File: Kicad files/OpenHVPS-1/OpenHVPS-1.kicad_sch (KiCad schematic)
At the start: 64 parts, among them J1 Conn_01x03_Male, Q1 FQT7N10, Q2 BC846, Q3 MMDT3906, U1 74HC14, U2 MAX4162, U3 CD14538BM, U4 MAX6008AEUR+T

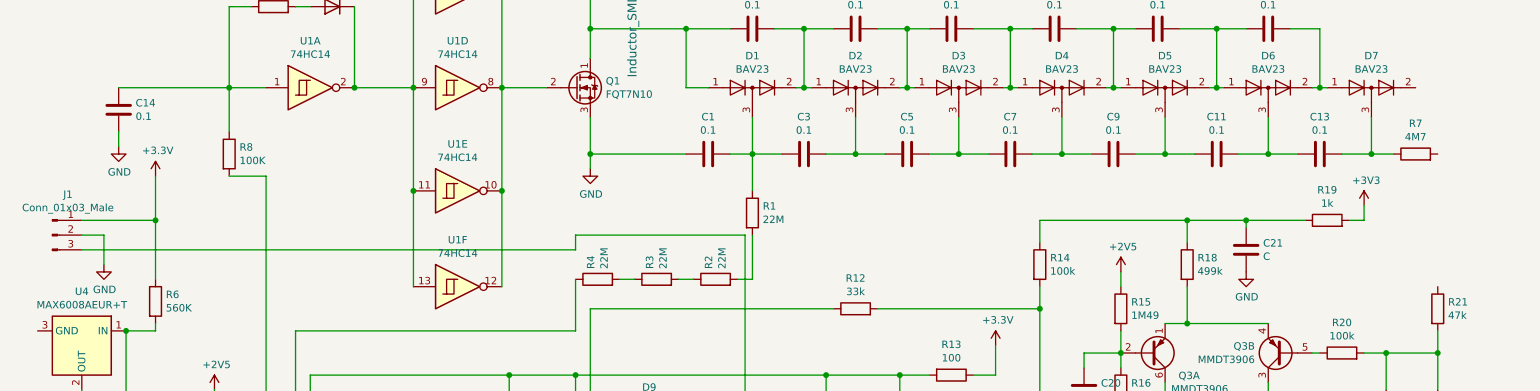
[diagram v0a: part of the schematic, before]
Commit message: Added extra outputs and A-C placement moved
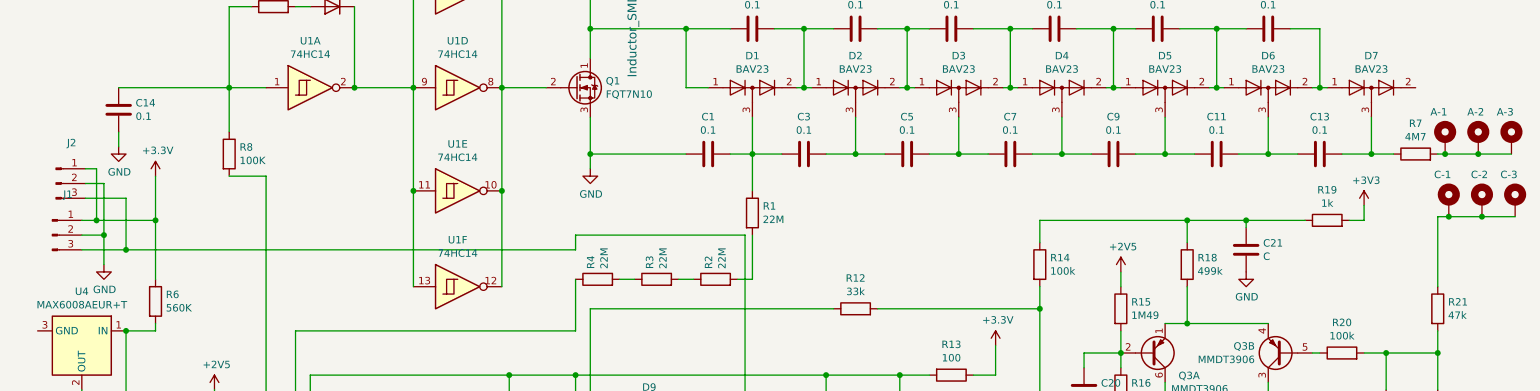
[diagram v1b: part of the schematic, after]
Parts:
- added H1: A-1, TestPoint:TestPoint_Loop_D1.80mm_Drill1.0mm_Beaded, symbol Mechanical:MountingHole_Pad
- added H2: C-1, TestPoint:TestPoint_Loop_D1.80mm_Drill1.0mm_Beaded, symbol Mechanical:MountingHole_Pad
- added H3: A-2, TestPoint:TestPoint_Loop_D2.60mm_Drill1.4mm_Beaded, symbol Mechanical:MountingHole_Pad
- added H4: C-2, TestPoint:TestPoint_Loop_D2.60mm_Drill1.4mm_Beaded, symbol Mechanical:MountingHole_Pad
- added H5: A-3, TestPoint:TestPoint_Loop_D3.80mm_Drill2.0mm, symbol Mechanical:MountingHole_Pad
- added H6: C-3, TestPoint:TestPoint_Loop_D3.80mm_Drill2.0mm, symbol Mechanical:MountingHole_Pad
- added J2: Conn_01x03_Male, Connector_PinHeader_2.54mm:PinHeader_1x03_P2.54mm_Vertical, symbol Connector:Conn_01x03_Male
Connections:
- net +3V3: now also J2.1 (Pin_1)
- net GND: now also J2.2 (Pin_2)
- net at D9.2 (A), J1.3 (Pin_3), U3.6 (Q): now also J2.3 (Pin_3)
- net at R7.2: now also H1.1, H3.1, H5.1
- net at R21.1: now also H2.1, H4.1, H6.1

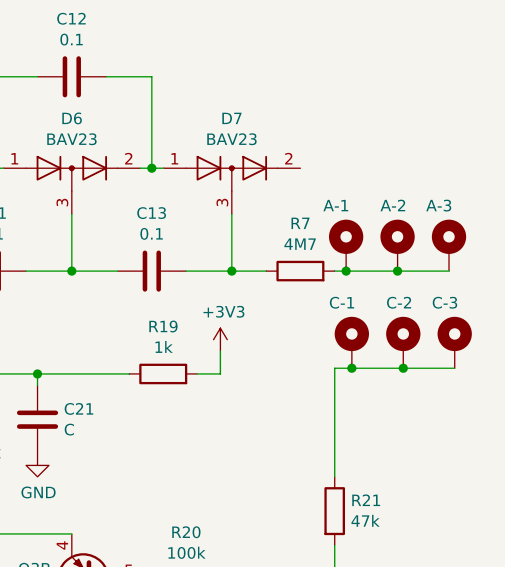
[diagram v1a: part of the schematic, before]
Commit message: changes to anode and cathode plus some parts layout, not routed!
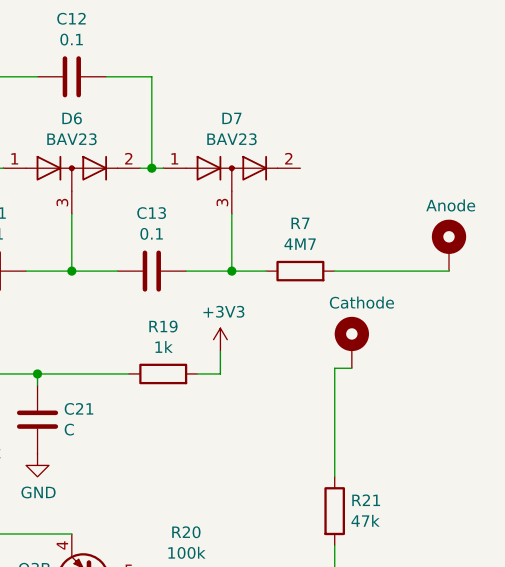
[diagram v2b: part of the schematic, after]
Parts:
- removed H1: A-1, TestPoint:TestPoint_Loop_D1.80mm_Drill1.0mm_Beaded, symbol Mechanical:MountingHole_Pad
- removed H3: A-2, TestPoint:TestPoint_Loop_D2.60mm_Drill1.4mm_Beaded, symbol Mechanical:MountingHole_Pad
- removed H4: C-2, TestPoint:TestPoint_Loop_D2.60mm_Drill1.4mm_Beaded, symbol Mechanical:MountingHole_Pad
- removed H6: C-3, TestPoint:TestPoint_Loop_D3.80mm_Drill2.0mm, symbol Mechanical:MountingHole_Pad
- H2: value C-1 -> Cathode; footprint TestPoint:TestPoint_Loop_D1.80mm_Drill1.0mm_Beaded -> TestPoint:TestPoint_Loop_D3.80mm_Drill2.0mm
- H5: value A-3 -> Anode
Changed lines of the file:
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@@
   (junction (at 257.81 135.89) (diameter 1.016) (color 0 0 0 0))
   (junction (at 257.81 152.4) (diameter 1.016) (color 0 0 0 0))
-  (junction (at 259.08 101.6) (diameter 1.016) (color 0 0 0 0))
-  (junction (at 259.715 112.395) (diameter 1.016) (color 0 0 0 0))
-  (junction (at 264.795 101.6) (diameter 1.016) (color 0 0 0 0))
-  (junction (at 265.43 112.395) (diameter 1.016) (color 0 0 0 0))
   (wire (pts (xy 24.13 113.03) (xy 26.67 113.03))
     (stroke (width 0) (type solid) (color 0 0 0 0))
@@
     (stroke (width 0) (type solid) (color 0 0 0 0))
   )
-  (wire (pts (xy 257.81 101.6) (xy 259.08 101.6))
+  (wire (pts (xy 257.81 101.6) (xy 270.51 101.6))
     (stroke (width 0) (type solid) (color 0 0 0 0))
   )
@@
   )
   (wire (pts (xy 257.81 152.4) (xy 257.81 156.21))
-    (stroke (width 0) (type solid) (color 0 0 0 0))
-  )
-  (wire (pts (xy 259.08 101.6) (xy 264.795 101.6))
-    (stroke (width 0) (type solid) (color 0 0 0 0))
-  )
-  (wire (pts (xy 259.715 112.395) (xy 265.43 112.395))
-    (stroke (width 0) (type solid) (color 0 0 0 0))
-  )
-  (wire (pts (xy 264.795 101.6) (xy 270.51 101.6))
-    (stroke (width 0) (type solid) (color 0 0 0 0))
-  )
-  (wire (pts (xy 265.43 112.395) (xy 271.145 112.395))
     (stroke (width 0) (type solid) (color 0 0 0 0))
   )
@@
     )
   )
-  (symbol (lib_id "Mechanical:MountingHole_Pad") (at 259.08 99.06 0) (unit 1)
-    (in_bom yes) (on_board yes)
-    (property "Reference" "H1" (id 0) (at 261.62 97.784 0)
-      (effects (font (size 1.27 1.27)) (justify left) hide)
-    )
-    (property "Value" "A-1" (id 1) (at 256.5401 94.3673 0)
-      (effects (font (size 1.27 1.27)) (justify left))
-    )
-    (property "Footprint" "TestPoint:TestPoint_Loop_D1.80mm_Drill1.0mm_Beaded" (id 2) (at 259.08 99.06 0)
-      (effects (font (size 1.27 1.27)) hide)
-    )
-    (property "Datasheet" "~" (id 3) (at 259.08 99.06 0)
-      (effects (font (size 1.27 1.27)) hide)
-    )
-  )
   (symbol (lib_id "Mechanical:MountingHole_Pad") (at 259.715 109.855 0) (unit 1)
     (in_bom yes) (on_board yes)
@@
       (effects (font (size 1.27 1.27)) (justify left) hide)
     )
-    (property "Value" "C-1" (id 1) (at 257.175 105.162 0)
-      (effects (font (size 1.27 1.27)) (justify left))
-    )
-    (property "Footprint" "TestPoint:TestPoint_Loop_D1.80mm_Drill1.0mm_Beaded" (id 2) (at 259.715 109.855 0)
+    (property "Value" "Cathode" (id 1) (at 257.175 105.162 0)
+      (effects (font (size 1.27 1.27)) (justify left))
+    )
+    (property "Footprint" "TestPoint:TestPoint_Loop_D3.80mm_Drill2.0mm" (id 2) (at 259.715 109.855 0)
       (effects (font (size 1.27 1.27)) hide)
     )
     (property "Datasheet" "~" (id 3) (at 259.715 109.855 0)
-      (effects (font (size 1.27 1.27)) hide)
-    )
-  )
-  (symbol (lib_id "Mechanical:MountingHole_Pad") (at 264.795 99.06 0) (unit 1)
-    (in_bom yes) (on_board yes)
-    (property "Reference" "H3" (id 0) (at 267.335 97.784 0)
-      (effects (font (size 1.27 1.27)) (justify left) hide)
-    )
-    (property "Value" "A-2" (id 1) (at 262.89 94.367 0)
-      (effects (font (size 1.27 1.27)) (justify left))
-    )
-    (property "Footprint" "TestPoint:TestPoint_Loop_D2.60mm_Drill1.4mm_Beaded" (id 2) (at 264.795 99.06 0)
-      (effects (font (size 1.27 1.27)) hide)
-    )
-    (property "Datasheet" "~" (id 3) (at 264.795 99.06 0)
-      (effects (font (size 1.27 1.27)) hide)
-    )
-  )
-  (symbol (lib_id "Mechanical:MountingHole_Pad") (at 265.43 109.855 0) (unit 1)
-    (in_bom yes) (on_board yes)
-    (property "Reference" "H4" (id 0) (at 267.97 108.579 0)
-      (effects (font (size 1.27 1.27)) (justify left) hide)
-    )
-    (property "Value" "C-2" (id 1) (at 263.525 105.162 0)
-      (effects (font (size 1.27 1.27)) (justify left))
-    )
-    (property "Footprint" "TestPoint:TestPoint_Loop_D2.60mm_Drill1.4mm_Beaded" (id 2) (at 265.43 109.855 0)
-      (effects (font (size 1.27 1.27)) hide)
-    )
-    (property "Datasheet" "~" (id 3) (at 265.43 109.855 0)
       (effects (font (size 1.27 1.27)) hide)
     )
@@
       (effects (font (size 1.27 1.27)) (justify left) hide)
     )
-    (property "Value" "A-3" (id 1) (at 267.97 94.367 0)
+    (property "Value" "Anode" (id 1) (at 267.97 94.367 0)
       (effects (font (size 1.27 1.27)) (justify left))
     )
@@
     )
     (property "Datasheet" "~" (id 3) (at 270.51 99.06 0)
-      (effects (font (size 1.27 1.27)) hide)
-    )
-  )
-  (symbol (lib_id "Mechanical:MountingHole_Pad") (at 271.145 109.855 0) (unit 1)
-    (in_bom yes) (on_board yes)
-    (property "Reference" "H6" (id 0) (at 273.685 108.579 0)
-      (effects (font (size 1.27 1.27)) (justify left) hide)
-    )
-    (property "Value" "C-3" (id 1) (at 268.605 105.162 0)
-      (effects (font (size 1.27 1.27)) (justify left))
-    )
-    (property "Footprint" "TestPoint:TestPoint_Loop_D3.80mm_Drill2.0mm" (id 2) (at 271.145 109.855 0)
-      (effects (font (size 1.27 1.27)) hide)
-    )
-    (property "Datasheet" "~" (id 3) (at 271.145 109.855 0)
       (effects (font (size 1.27 1.27)) hide)
     )
@@
       (reference "FB2") (unit 1) (value "Ferrite_Bead") (footprint "Resistor_SMD:R_0805_2012Metric")
     )
-    (path "/711dab73-9579-4541-8dd9-06f41ce53f6b"
-      (reference "H1") (unit 1) (value "A-1") (footprint "TestPoint:TestPoint_Loop_D1.80mm_Drill1.0mm_Beaded")
-    )
     (path "/5534fd63-59cd-4e2a-9176-13a9cbe98172"
-      (reference "H2") (unit 1) (value "C-1") (footprint "TestPoint:TestPoint_Loop_D1.80mm_Drill1.0mm_Beaded")
-    )
-    (path "/a55a93d9-bca5-44d8-a006-44ca18ff56c0"
-      (reference "H3") (unit 1) (value "A-2") (footprint "TestPoint:TestPoint_Loop_D2.60mm_Drill1.4mm_Beaded")
-    )
-    (path "/6454c411-40ae-4d15-8805-ce33fb8c2c9c"
-      (reference "H4") (unit 1) (value "C-2") (footprint "TestPoint:TestPoint_Loop_D2.60mm_Drill1.4mm_Beaded")
+      (reference "H2") (unit 1) (value "Cathode") (footprint "TestPoint:TestPoint_Loop_D3.80mm_Drill2.0mm")
     )
     (path "/8e6f414f-5055-45b6-9d50-4d4f2e754637"
-      (reference "H5") (unit 1) (value "A-3") (footprint "TestPoint:TestPoint_Loop_D3.80mm_Drill2.0mm")
-    )
-    (path "/d4df23bd-4f19-483c-9d8c-226374b00a1f"
-      (reference "H6") (unit 1) (value "C-3") (footprint "TestPoint:TestPoint_Loop_D3.80mm_Drill2.0mm")
+      (reference "H5") (unit 1) (value "Anode") (footprint "TestPoint:TestPoint_Loop_D3.80mm_Drill2.0mm")
     )
     (path "/0c63c58a-8bcb-4bdc-b09f-423326af1a5e"
